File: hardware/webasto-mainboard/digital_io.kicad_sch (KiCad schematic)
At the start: 34 parts, among them Q10 DMG2301L, Q2 2N7002, Q3 2N7002, Q4 2N7002, Q5 2N7002, Q6 SUD50P04-08, Q7 SUD50P04-08, Q8 SUD50P04-08, Q9 SUD50P04-08, U4 MC33660BEFR2

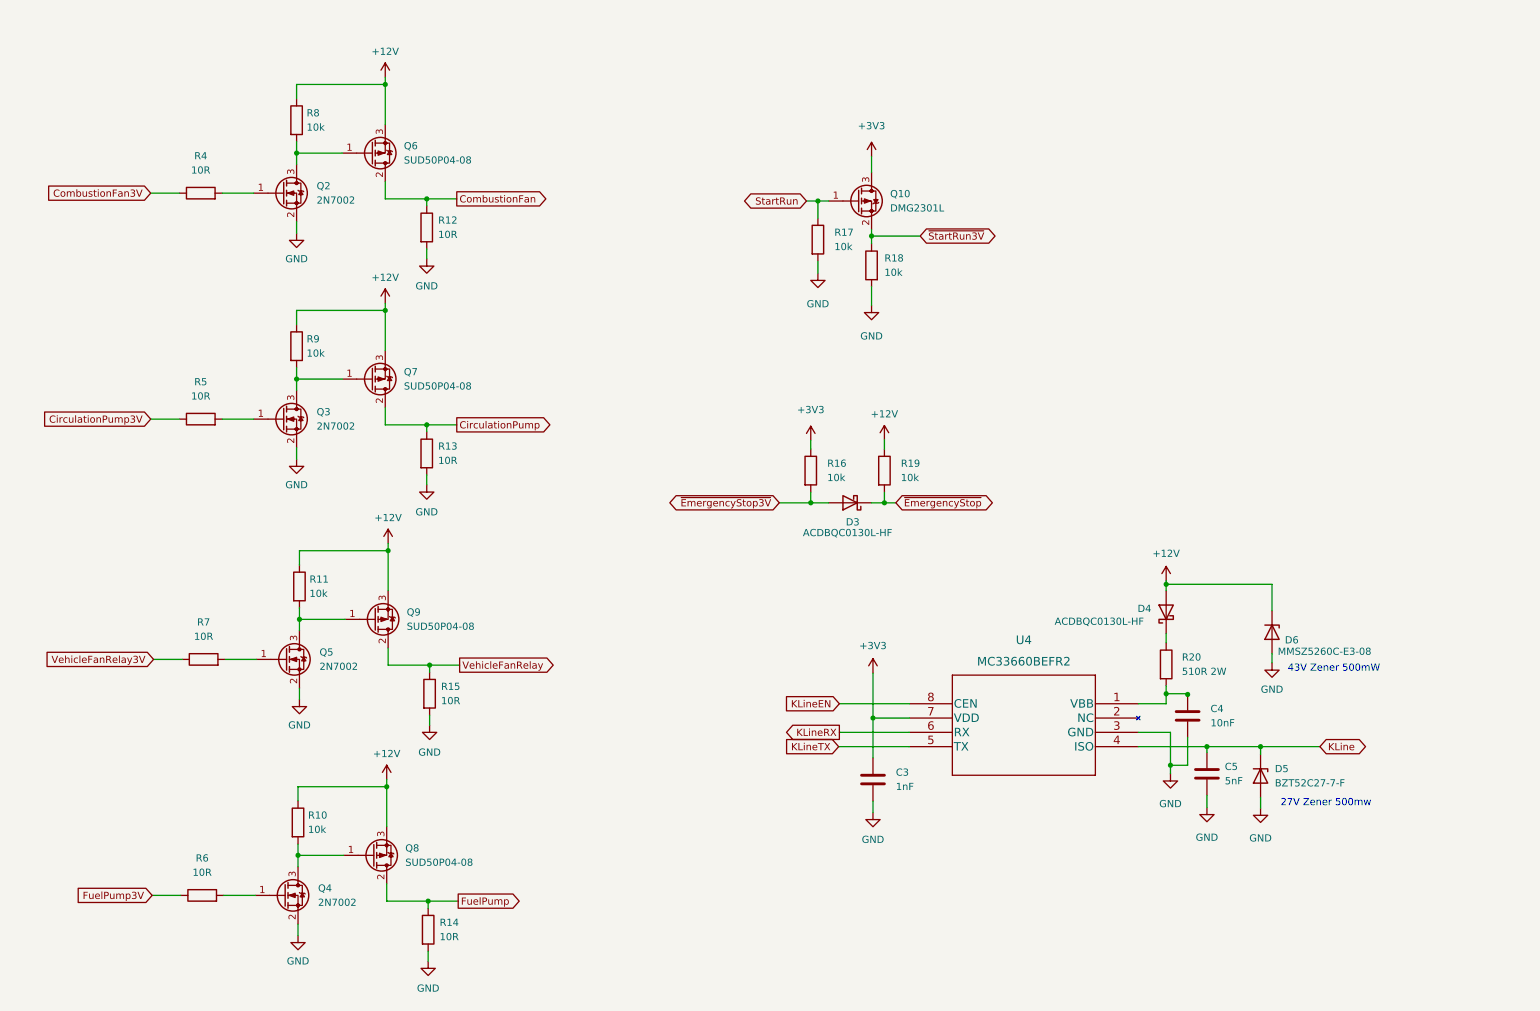
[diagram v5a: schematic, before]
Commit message: Added snubbing diodes on all the inputs
- back EMF from relays... I forgot...  so reverse biased diodes from
  GND to signal and from signal to +12V.
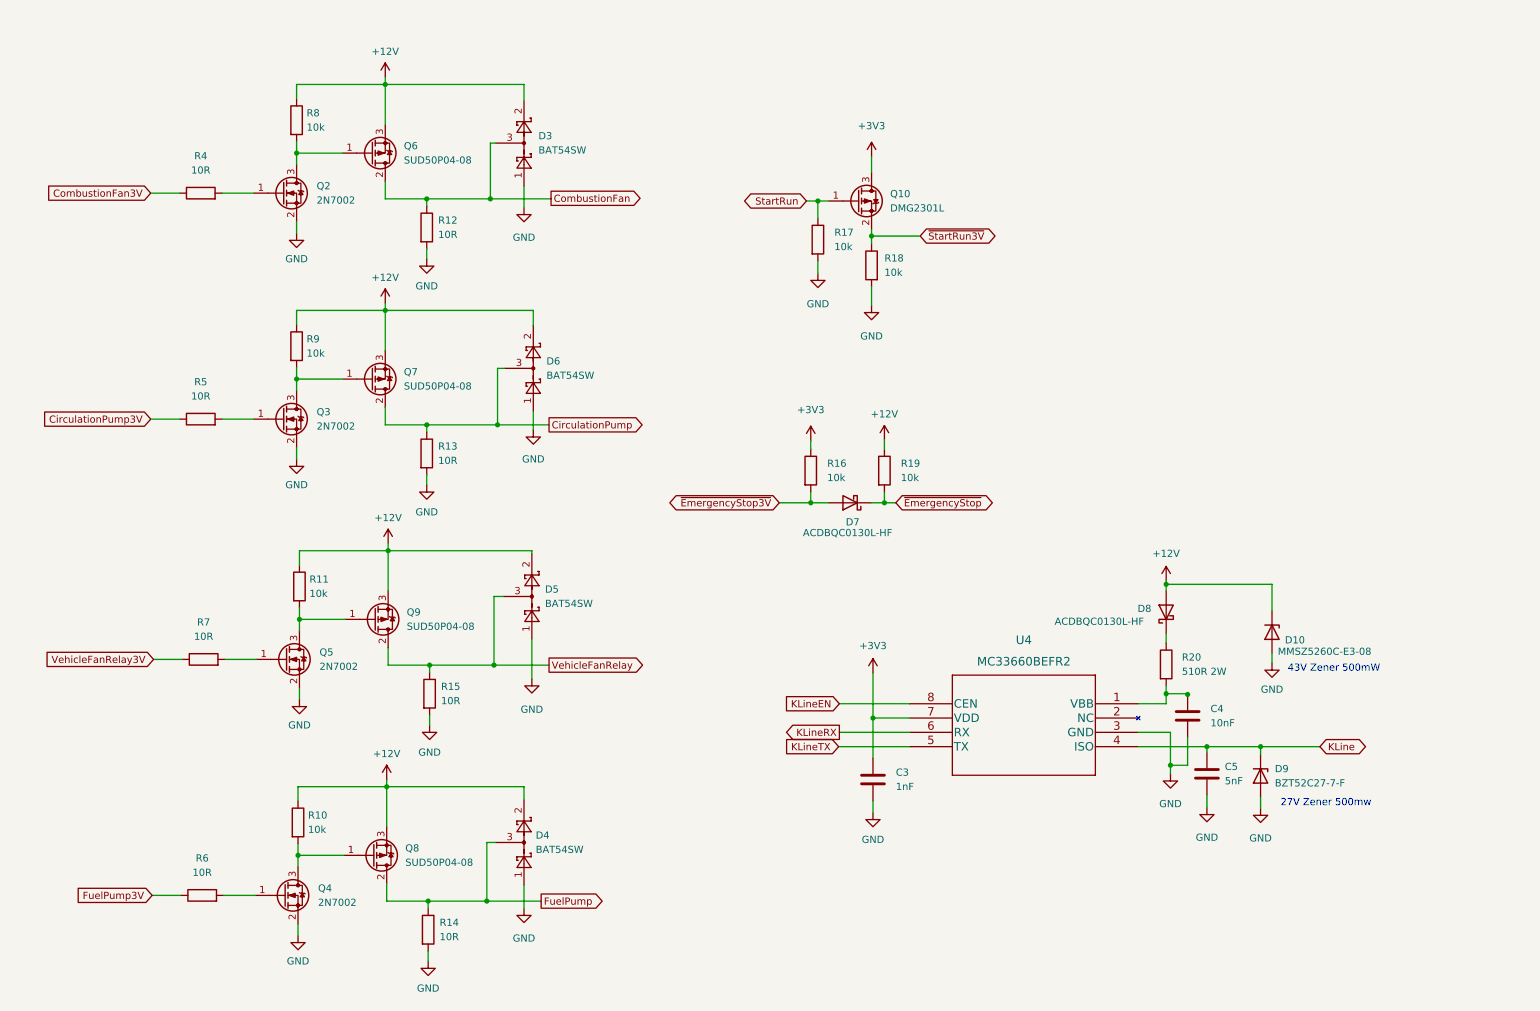
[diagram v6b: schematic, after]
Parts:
- added D3, D4, D5, D6: BAT54SW, Package_TO_SOT_SMD:SOT-323_SC-70, symbol Diode:BAT54SW
- renumbered D6 to D10, D3 to D7, D4 to D8, D5 to D9
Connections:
- net +12V: now also D3.2, D4.2, D5.2, D6.2
- net CirculationPump: now also D6.3
- net CombustionFan: now also D3.3
- net FuelPump: now also D4.3
- net GND: now also D3.1, D4.1, D5.1, D6.1
- net VehicleFanRelay: now also D5.3

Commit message: Update title block on mainboard, print PDFs
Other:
- company: (none) -> Gavin Hurlbut
- title: Webasto Thermo Top C Replacement Controller -> Webasto Replacement Mainboard (Thermo Top C)
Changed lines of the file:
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@@
   (paper "A4")
   (title_block
-    (title "Webasto Thermo Top C Replacement Controller")
-    (date "2023-01-19")
+    (title "Webasto Replacement Mainboard (Thermo Top C)")
+    (date "2023-01-31")
     (rev "v1.0")
+    (company "Gavin Hurlbut")
   )
   (junction (at 68.072 121.158) (diameter 0) (color 0 0 0 0)

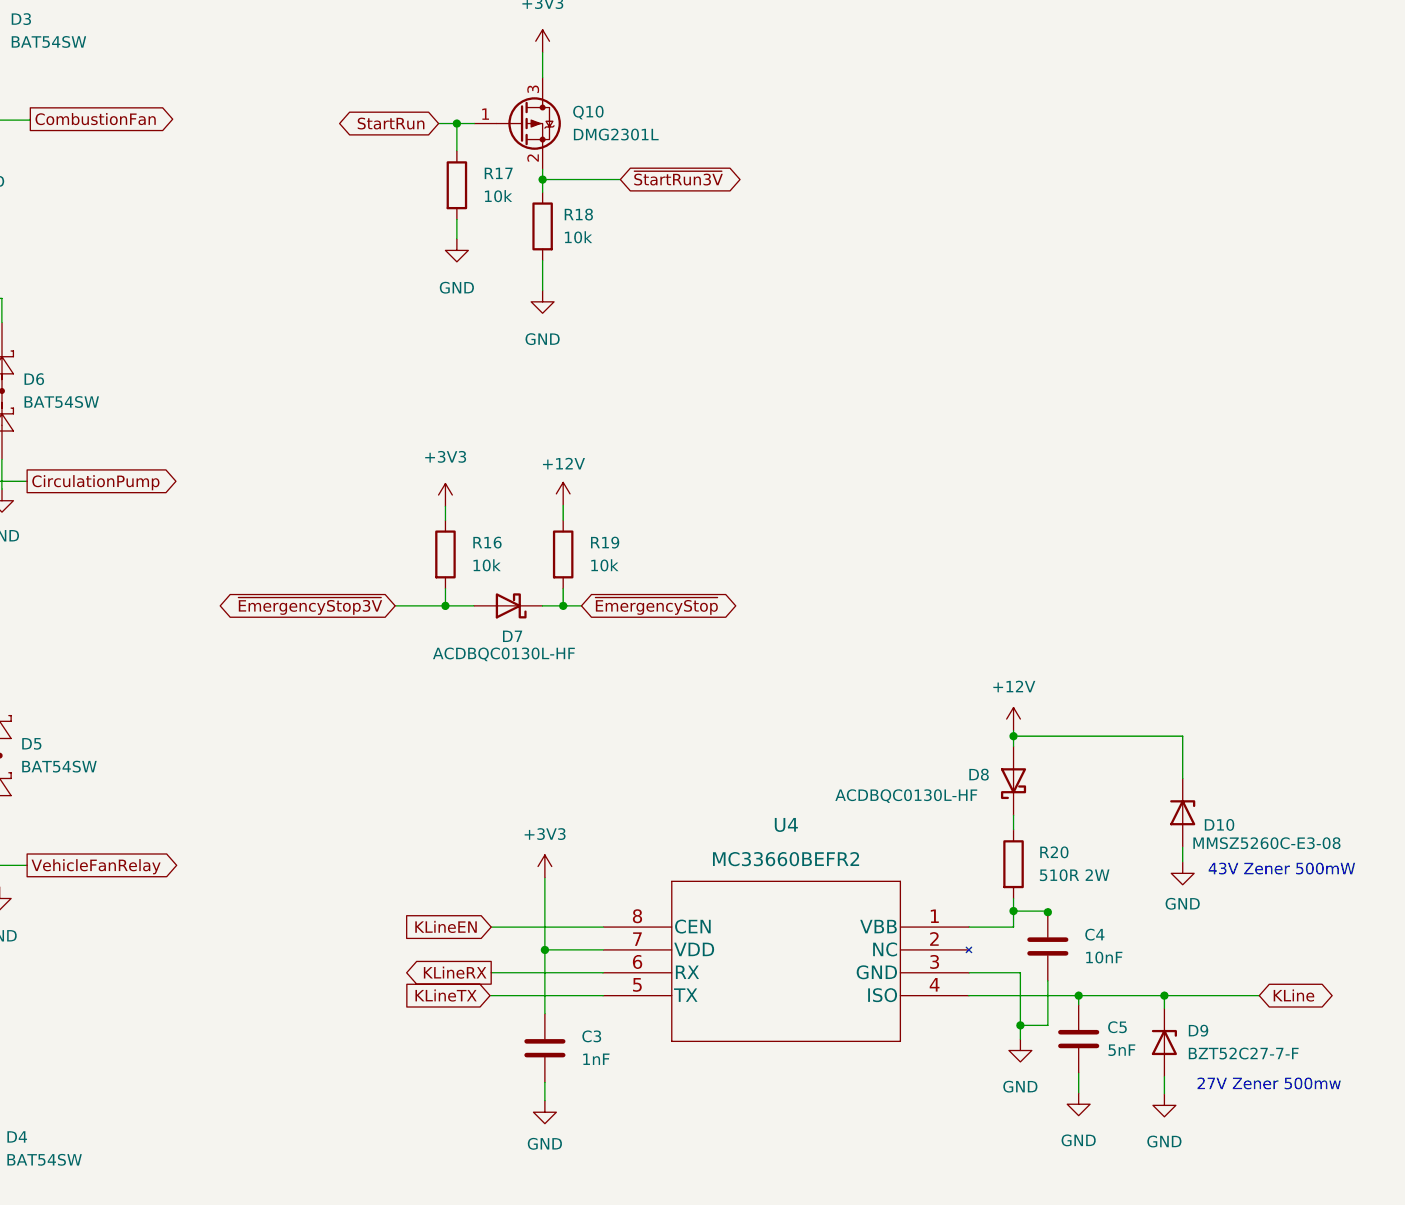
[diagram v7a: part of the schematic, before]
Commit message: Moved emerg. shutdown offboard
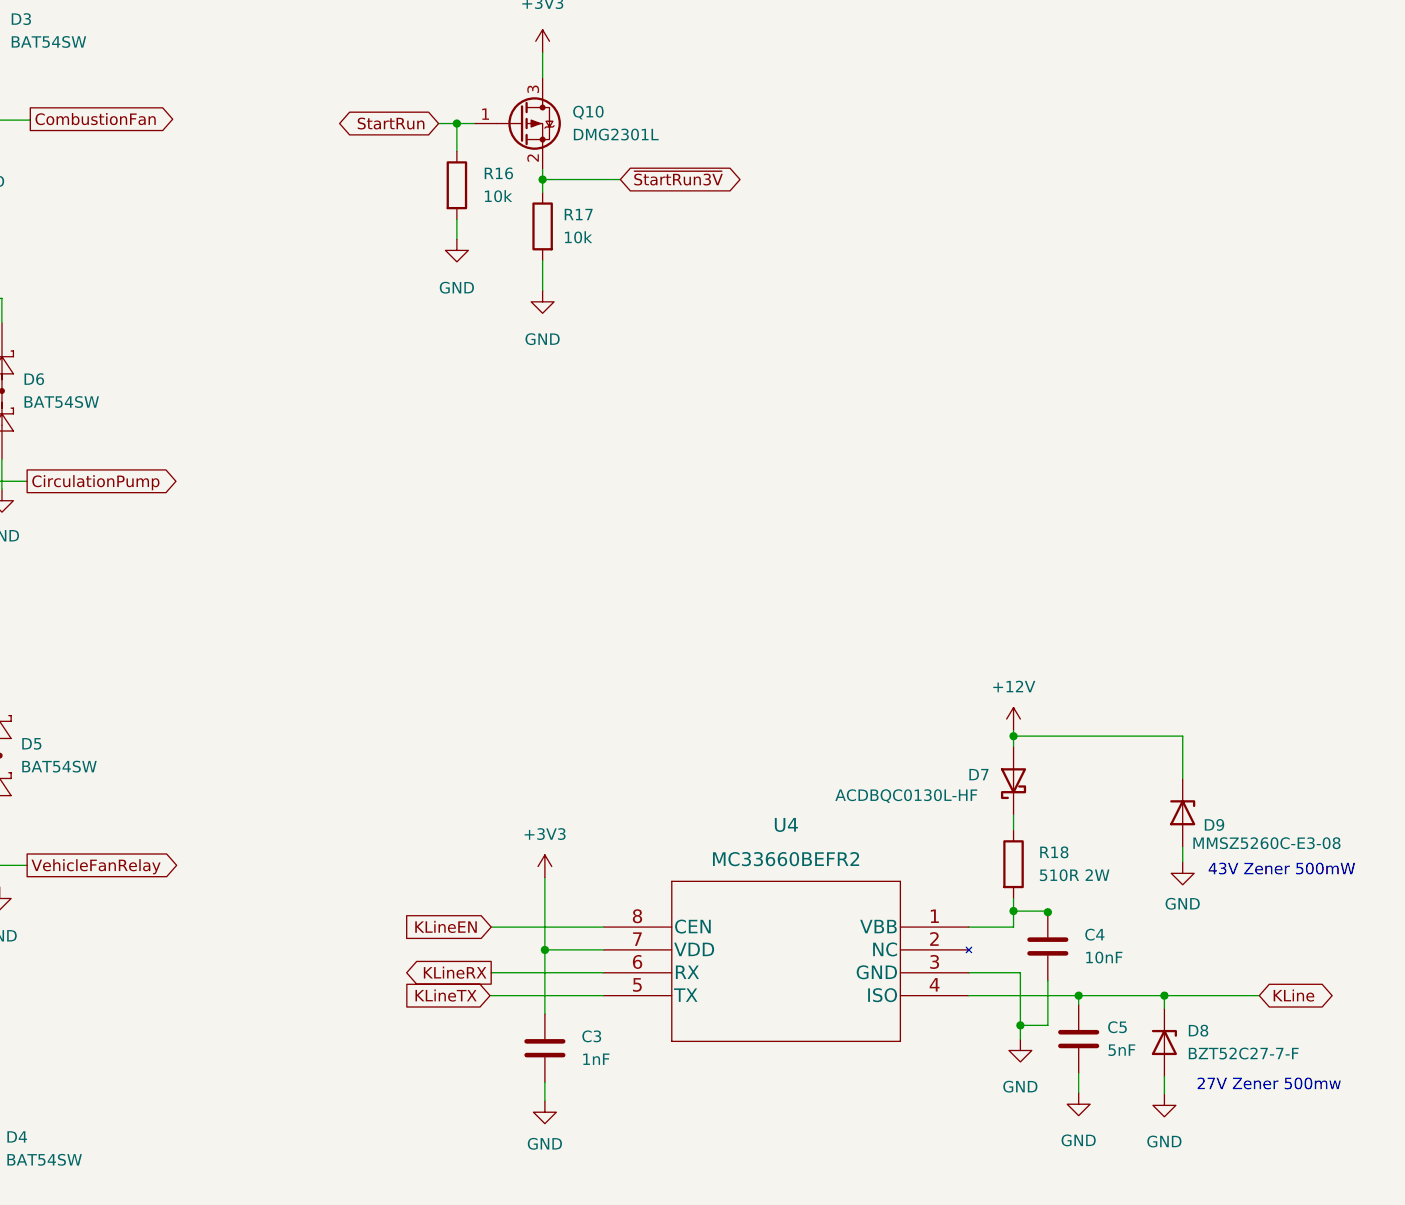
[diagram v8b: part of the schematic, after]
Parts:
- removed D7: ACDBQC0130L-HF, Diode_SMD:D_SOD-923, symbol Device:D_Schottky
- removed R16, R19: 10k, Resistor_SMD:R_0805_2012Metric_Pad1.20x1.40mm_HandSolder, symbol Device:R
- renumbered D8 to D7, D9 to D8, D10 to D9, R17 to R16, R18 to R17, R20 to R18
